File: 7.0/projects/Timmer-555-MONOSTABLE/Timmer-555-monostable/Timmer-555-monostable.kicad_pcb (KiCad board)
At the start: 2 copper layers, 70.5 x 63.5 mm, 8 parts, among them SW0 SW_SWITCH, SW1 SW_Push, U1 LM555xM

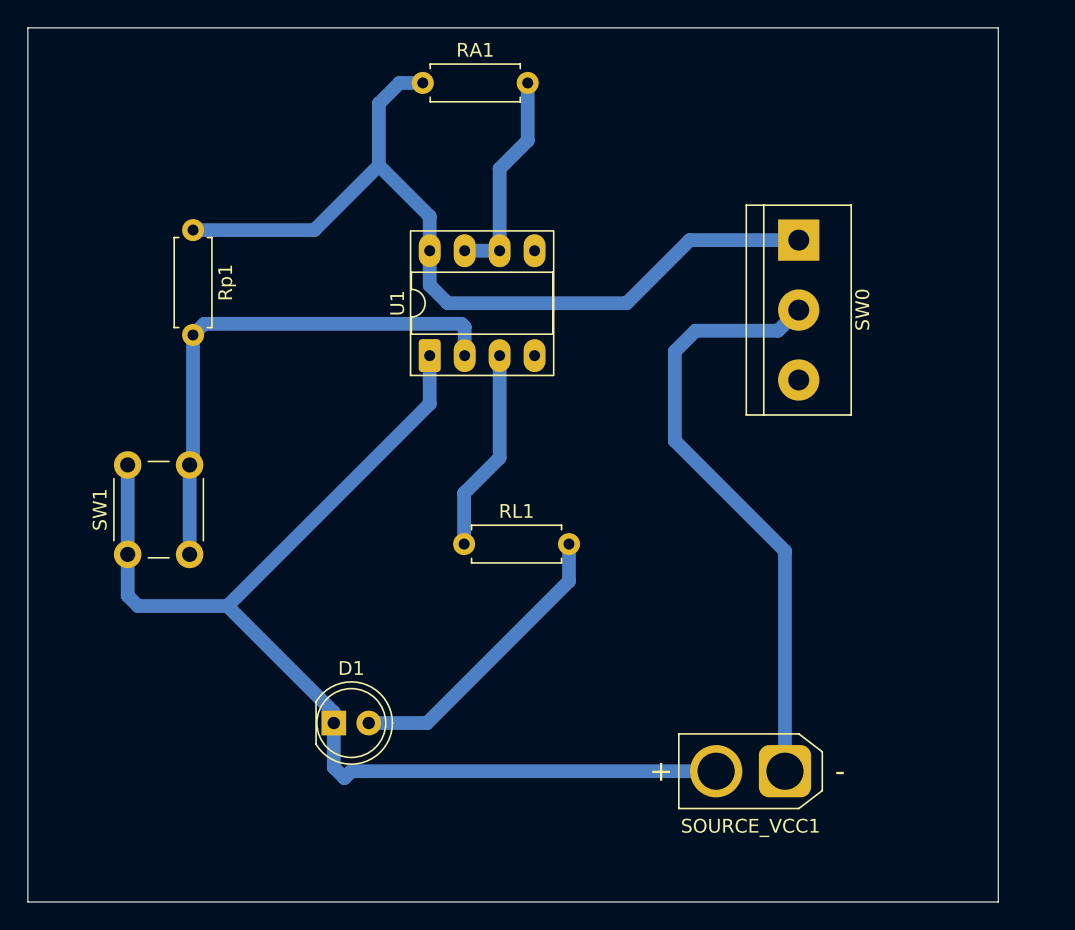
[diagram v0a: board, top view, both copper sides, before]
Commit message: adding 555-monostable ok
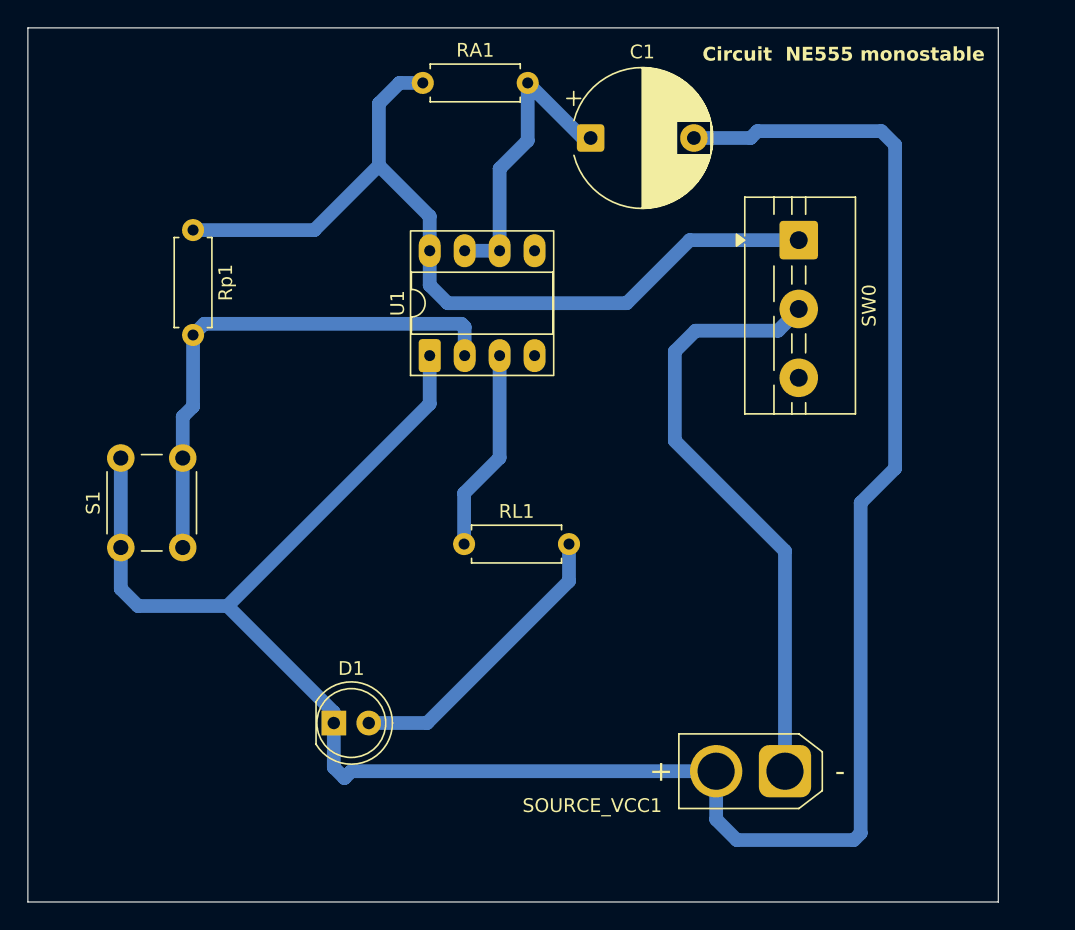
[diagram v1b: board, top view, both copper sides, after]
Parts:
- removed SW1: SW_Push, Button_Switch_THT:SW_PUSH_6mm_H5mm
- added C1: 100uF, Capacitor_THT:CP_Radial_D10.0mm_P7.50mm, F.Cu at (131.4, 31.0)
- added S1: SW_Push, Button_Switch_THT:SW_PUSH_6mm_H5mm, F.Cu at (97.2, 60.8)
- SW0: footprint TerminalBlock:TerminalBlock_bornier-3_P5.08mm -> TerminalBlock:TerminalBlock_MaiXu_MX126-5.0-03P_1x03_P5.00mm
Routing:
- net GND: track 84.6 -> 166.7 mm
- net THR: track 15.6 -> 21.8 mm
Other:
- board text added: "Circuit NE555 monostable"

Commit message: adding goog values for 555 project
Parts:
- C1: value 100uF -> 270uF
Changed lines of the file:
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@@
 			)
 		)
-		(property "Value" "100uF"
+		(property "Value" "270uF"
 			(at 3.75 6.25 0)
 			(layer "F.Fab")
